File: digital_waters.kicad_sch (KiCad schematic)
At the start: 0 parts

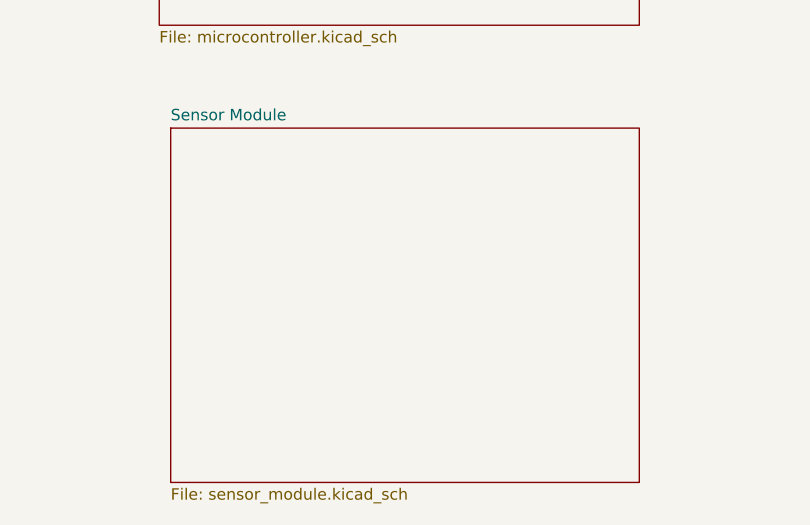
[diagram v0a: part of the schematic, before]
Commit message: Sensor board basic updates
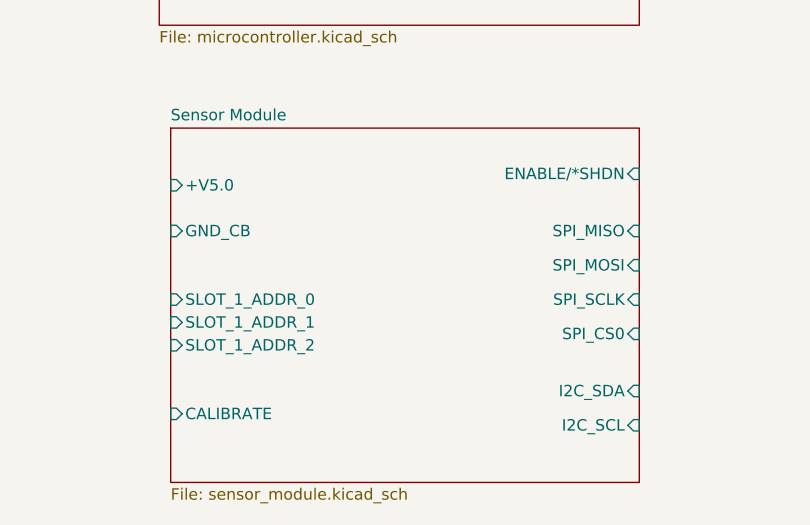
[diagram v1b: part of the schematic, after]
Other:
- sheet Sensor Module ports: added +V5.0, CALIBRATE, ENABLE/*SHDN, GND_CB, I2C_SCL, I2C_SDA, SLOT_1_ADDR_0, SLOT_1_ADDR_1, SLOT_1_ADDR_2, SPI_CS0, SPI_MISO, SPI_MOSI, SPI_SCLK; removed none
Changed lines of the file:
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@@
+			)
+		)
+		(pin "I2C_SDA" input
+			(at 179.07 110.49 0)
+			(effects
+				(font
+					(size 1.27 1.27)
+				)
+				(justify right)
+			)
+		)
+		(pin "I2C_SCL" input
+			(at 179.07 114.3 0)
+			(effects
+				(font
+					(size 1.27 1.27)
+				)
+				(justify right)
+			)
+		)
+		(pin "CALIBRATE" input
+			(at 127 113.03 180)
+			(effects
+				(font
+					(size 1.27 1.27)
+				)
+				(justify left)
+			)
+		)
+		(pin "SPI_SCLK" input
+			(at 179.07 100.33 0)
+			(effects
+				(font
+					(size 1.27 1.27)
+				)
+				(justify right)
+			)
+		)
+		(pin "SPI_CS0" input
+			(at 179.07 104.14 0)
+			(effects
+				(font
+					(size 1.27 1.27)
+				)
+				(justify right)
+			)
+		)
+		(pin "SPI_MOSI" input
+			(at 179.07 96.52 0)
+			(effects
+				(font
+					(size 1.27 1.27)
+				)
+				(justify right)
+			)
+		)
+		(pin "SPI_MISO" input
+			(at 179.07 92.71 0)
+			(effects
+				(font
+					(size 1.27 1.27)
+				)
+				(justify right)
+			)
+		)
+		(pin "GND_CB" input
+			(at 127 92.71 180)
+			(effects
+				(font
+					(size 1.27 1.27)
+				)
+				(justify left)
+			)
+		)
+		(pin "ENABLE{slash}*SHDN" input
+			(at 179.07 86.36 0)
+			(effects
+				(font
+					(size 1.27 1.27)
+				)
+				(justify right)
+			)
+		)
+		(pin "+V5.0" input
+			(at 127 87.63 180)
+			(effects
+				(font
+					(size 1.27 1.27)
+				)
+				(justify left)
+			)
+		)
+		(pin "SLOT_1_ADDR_0" input
+			(at 127 100.33 180)
+			(effects
+				(font
+					(size 1.27 1.27)
+				)
+				(justify left)
+			)
+		)
+		(pin "SLOT_1_ADDR_2" input
+			(at 127 105.41 180)
+			(effects
+				(font
+					(size 1.27 1.27)
+				)
+				(justify left)
+			)
+		)
+		(pin "SLOT_1_ADDR_1" input
+			(at 127 102.87 180)
+			(effects
+				(font
+					(size 1.27 1.27)
+				)
+				(justify left)
 			)
 		)

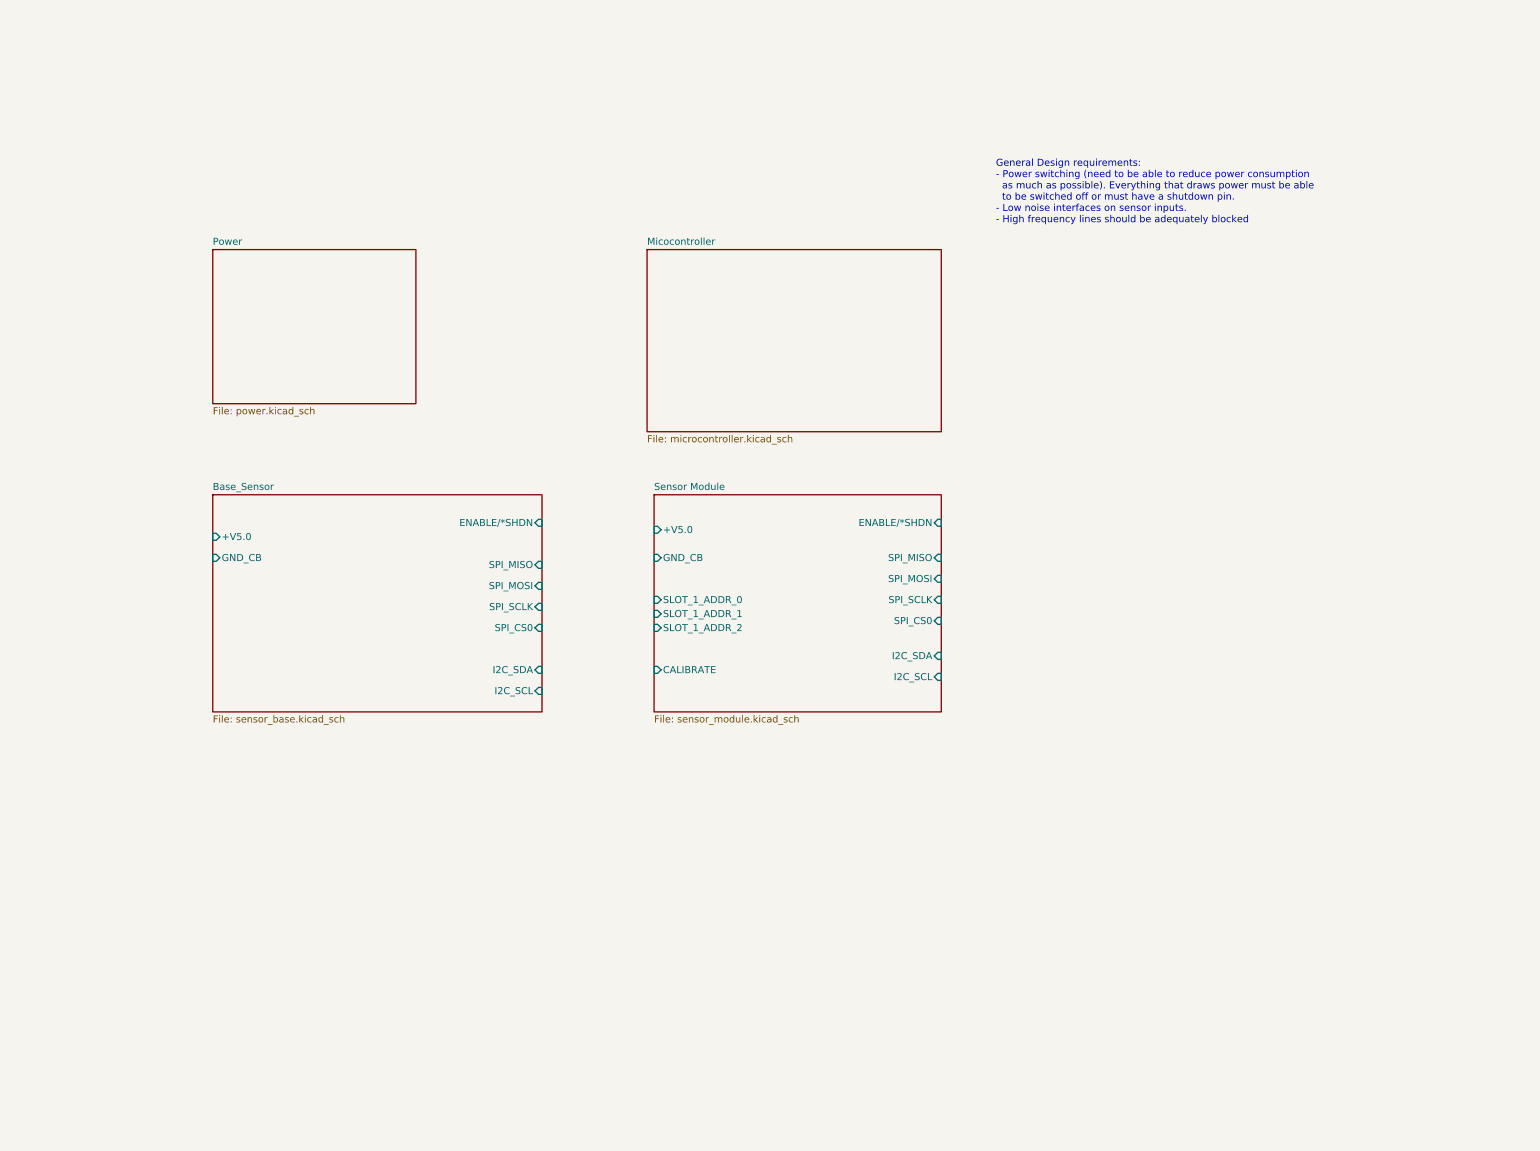
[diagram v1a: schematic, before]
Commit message: Split the sensor modules into a 4 and 8 port version. Fleshed out the power module a bit more. Started adding sensor board connectors to the root schematic and started pulling out sensor boards to their own, separate module. Began wiring up the root schematic to get my bearings a bit.
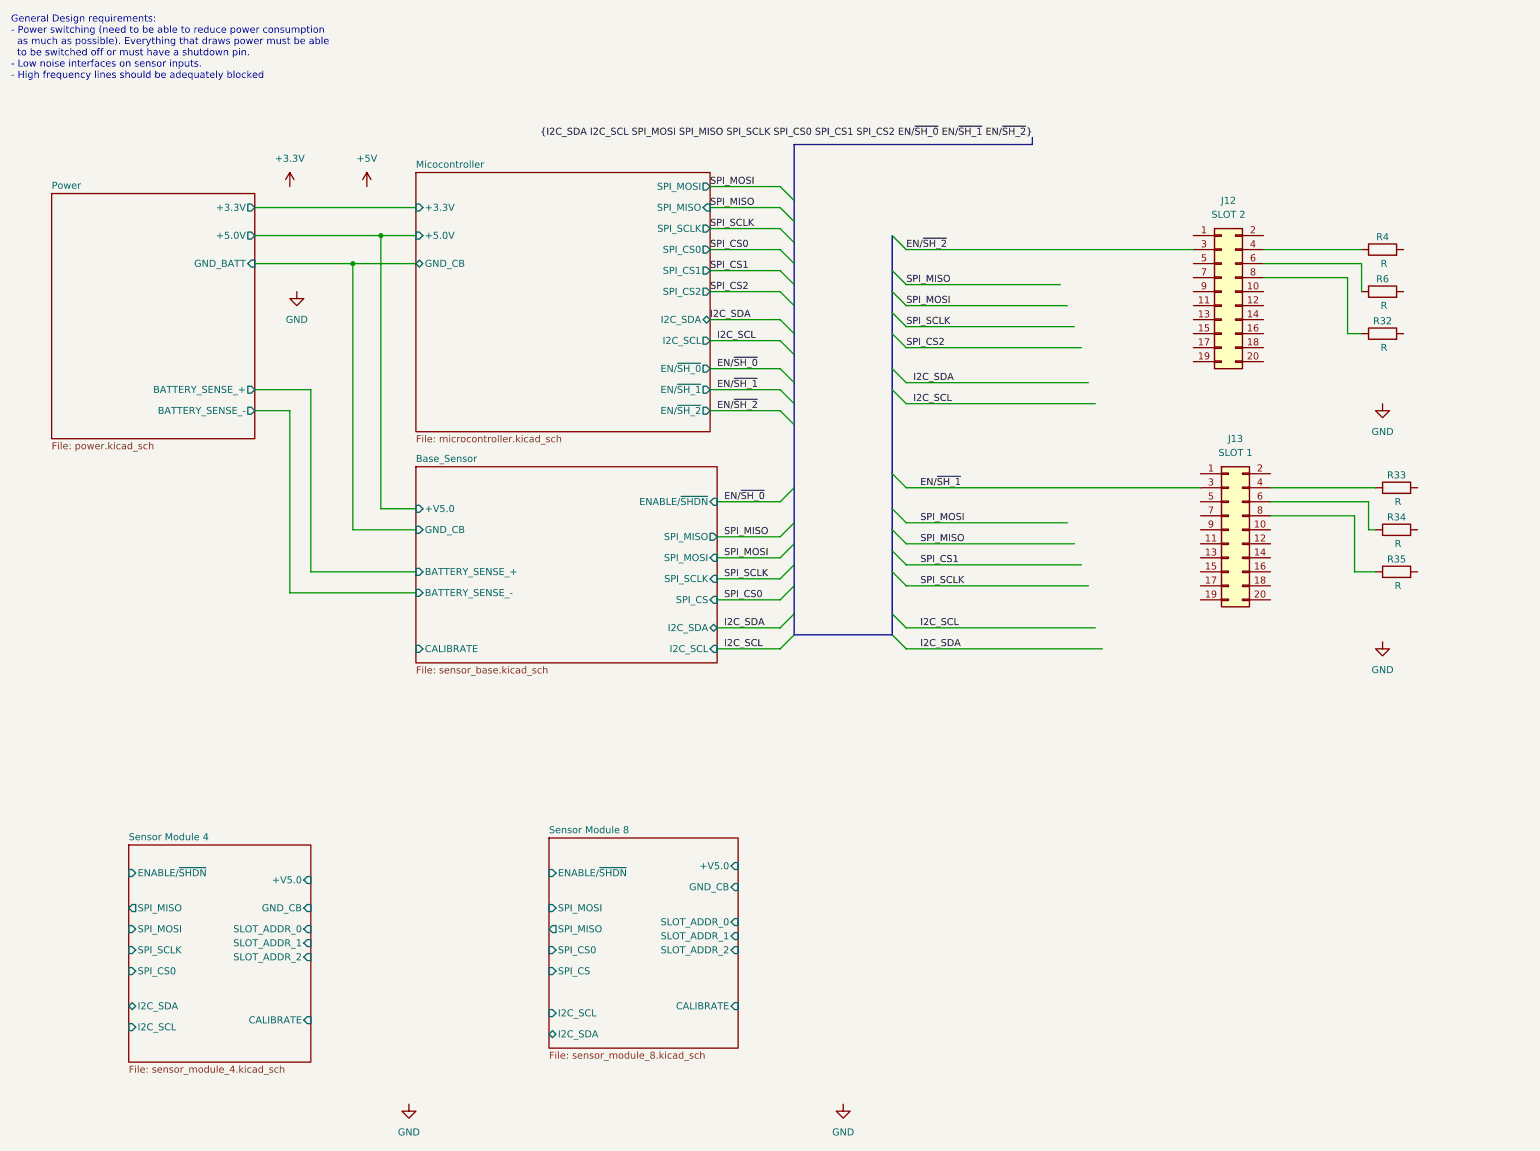
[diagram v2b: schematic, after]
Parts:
- added J12: SLOT 2, symbol Connector_Generic:Conn_02x10_Odd_Even
- added J13: SLOT 1, symbol Connector_Generic:Conn_02x10_Odd_Even
- added R32, R33, R34, R35, R4, R6: R, symbol Device:R
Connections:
- new net: J12.6 (Pin_6), R6.1
- new net: J13.8 (Pin_8), R35.1
- new net: J12.4 (Pin_4), R4.1
- new net: J12.8 (Pin_8), R32.1
- new net: J13.4 (Pin_4), R33.1
- new net: J13.6 (Pin_6), R34.1
- new net EN/~{SH_1}: J13.3 (Pin_3)
- new net EN/~{SH_2}: J12.3 (Pin_3)
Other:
- sheet Sensor Module renamed Sensor Module 4
- added sheet Sensor Module 8 (sensor_module_8.kicad_sch)
- sheet Base_Sensor ports: added BATTERY_SENSE_+, BATTERY_SENSE_-, CALIBRATE, ENABLE/~{SHDN}, SPI_CS; removed ENABLE/*SHDN, SPI_CS0
- sheet Micocontroller ports: added +3.3V, +5.0V, EN/~{SH_0}, EN/~{SH_1}, EN/~{SH_2}, GND_CB, I2C_SCL, I2C_SDA, SPI_CS0, SPI_CS1, SPI_CS2, SPI_MISO, SPI_MOSI, SPI_SCLK; removed none
- sheet Power ports: added +3.3V, +5.0V, BATTERY_SENSE_+, BATTERY_SENSE_-, GND_BATT; removed none
- sheet Sensor Module 4: file sensor_module.kicad_sch -> sensor_module_4.kicad_sch
- sheet Sensor Module 4 ports: added ENABLE/~{SHDN}, SLOT_ADDR_0, SLOT_ADDR_1, SLOT_ADDR_2; removed ENABLE/*SHDN, SLOT_1_ADDR_0, SLOT_1_ADDR_1, SLOT_1_ADDR_2

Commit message: Removed hierarchical labels on the sensor board (4 slot) in favour of local labels and connectors. The idea was that the sensor boards are plug-ins so having them defined as separate boards makes more sense. Eventually I think we'll pull them out of the main schematic and design each one separately with the common connector pinout.
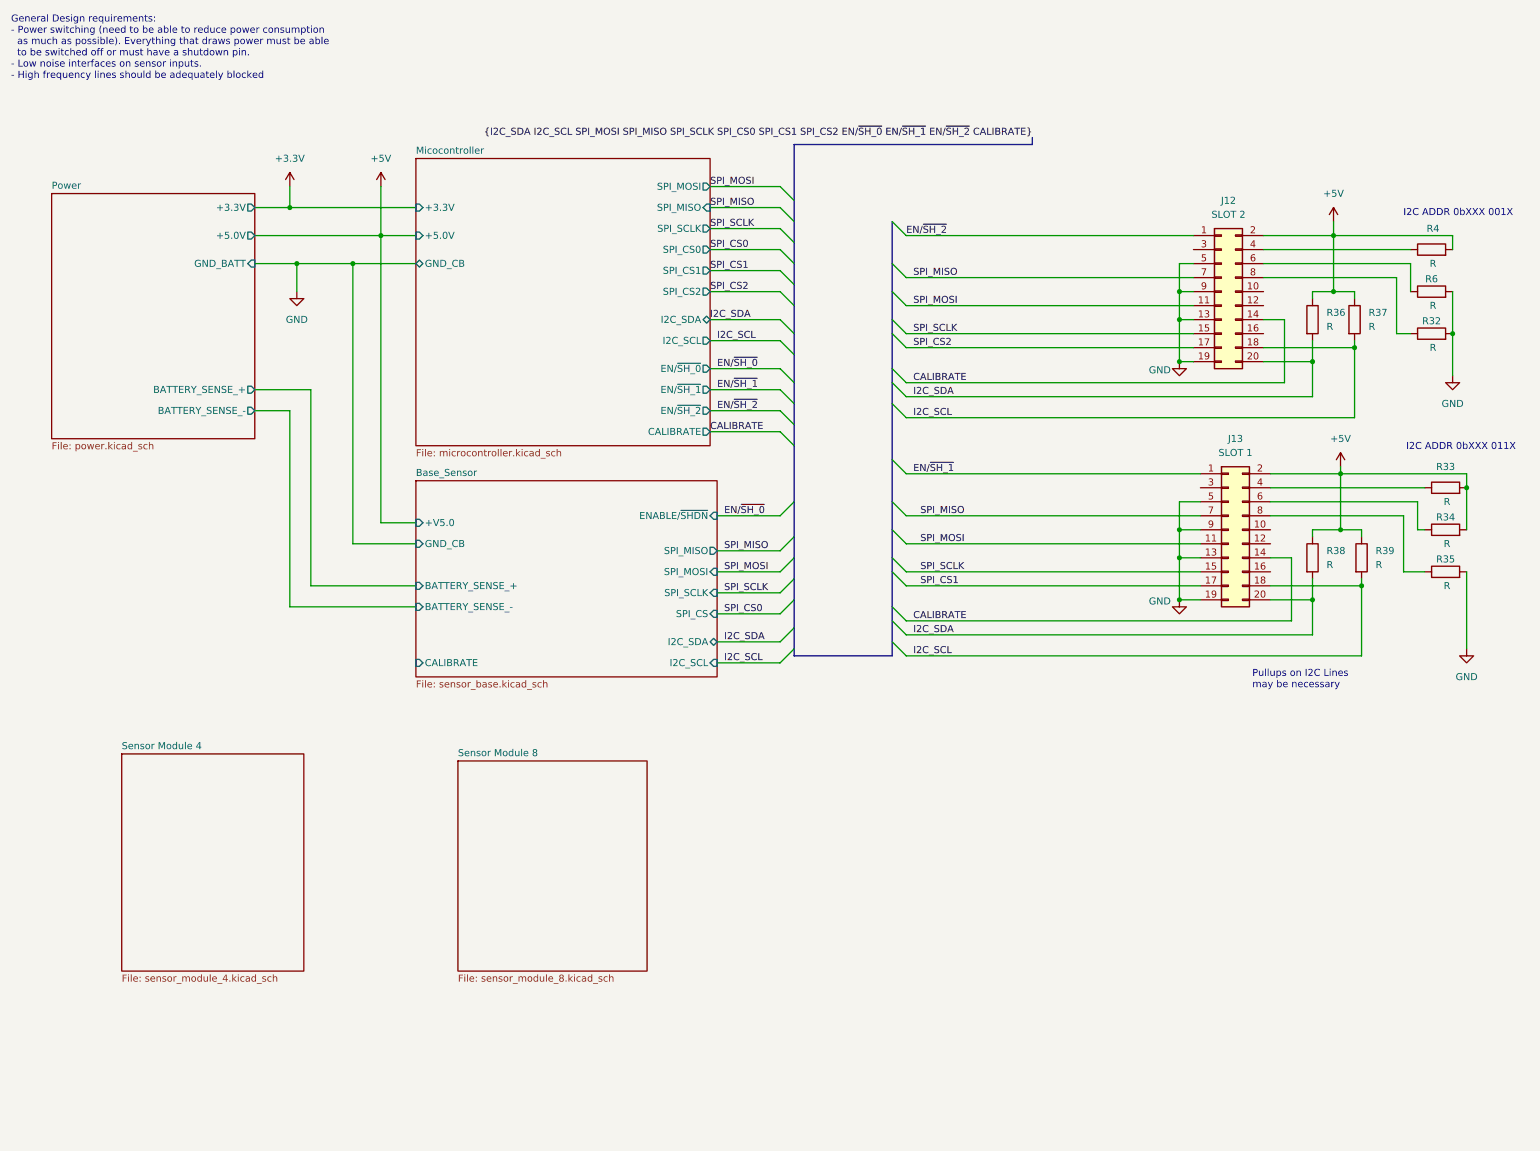
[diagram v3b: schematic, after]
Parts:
- added R36, R37, R38, R39: R, symbol Device:R
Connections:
- net +5V: now also J12.2 (Pin_2), J13.2 (Pin_2), R33.2, R34.2, R4.2, R36.1, R37.1, R38.1, R39.1
- net EN/~{SH_1}: now also J13.1 (Pin_1); no longer J13.3 (Pin_3)
- net EN/~{SH_2}: now also J12.1 (Pin_1); no longer J12.3 (Pin_3)
- net GND: now also J12.13 (Pin_13), J12.19 (Pin_19), J12.5 (Pin_5), J12.9 (Pin_9), J13.13 (Pin_13), J13.19 (Pin_19), J13.5 (Pin_5), J13.9 (Pin_9), R32.2, R35.2, R6.2
- net I2C_SCL: now also J12.18 (Pin_18), J13.18 (Pin_18), R37.2, R39.2
- net I2C_SDA: now also J12.20 (Pin_20), J13.20 (Pin_20), R36.2, R38.2
- net SPI_CS1: now also J13.17 (Pin_17)
- net SPI_CS2: now also J12.17 (Pin_17)
- net SPI_MISO: now also J12.7 (Pin_7), J13.7 (Pin_7)
- net SPI_MOSI: now also J12.11 (Pin_11), J13.11 (Pin_11)
- net SPI_SCLK: now also J12.15 (Pin_15), J13.15 (Pin_15)
- net CALIBRATE: now reaches J12.14 (Pin_14)
- net CALIBRATE: now also J13.14 (Pin_14)
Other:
- sheet Micocontroller ports: added CALIBRATE; removed none
- sheet Sensor Module 4 ports: added none; removed +V5.0, CALIBRATE, ENABLE/~{SHDN}, GND_CB, I2C_SCL, I2C_SDA, SLOT_ADDR_0, SLOT_ADDR_1, SLOT_ADDR_2, SPI_CS0, SPI_MISO, SPI_MOSI, SPI_SCLK
- sheet Sensor Module 8 ports: added none; removed +V5.0, CALIBRATE, ENABLE/~{SHDN}, GND_CB, I2C_SCL, I2C_SDA, SLOT_ADDR_0, SLOT_ADDR_1, SLOT_ADDR_2, SPI_CS, SPI_CS0, SPI_MISO, SPI_MOSI
- note added: "I2C ADDR 0bXXX 001X"
- note added: "I2C ADDR 0bXXX 011X"
- note added: "Pullups on I2C Lines may be necessary"
- moved on the sheet: R32, R33, R34, R35, R4, R6

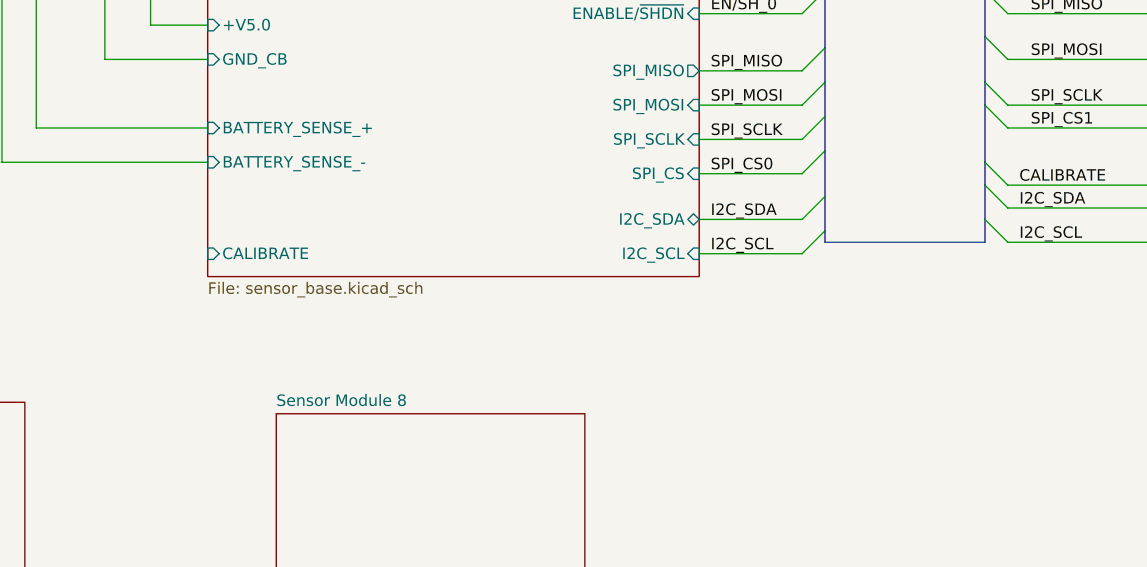
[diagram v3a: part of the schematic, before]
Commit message: Cleaned up some signal lines in the sensor board. Shuffled the decoupling caps around a bit as well as rearranged the EEPROM and power supply for clarity. Added buffered 2.5V offset to the pH and ORP circuits. Swapped one TBD input on the base sensor and sensor_4 boards for an ADC calibration input.
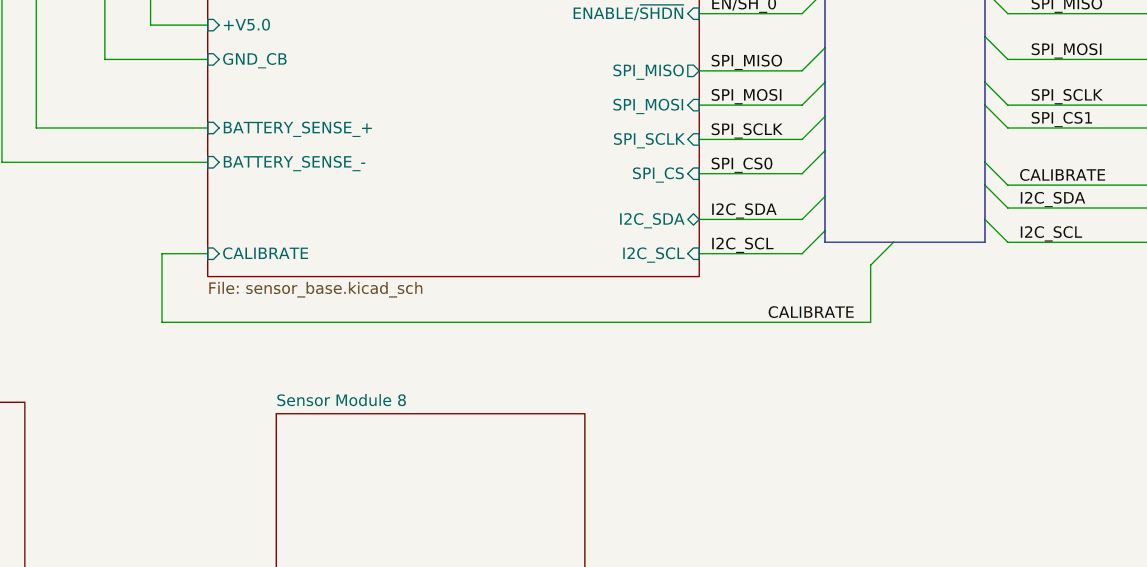
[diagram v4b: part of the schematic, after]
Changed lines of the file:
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@@
+	)
+	(bus_entry
+		(at 160.02 110.49)
+		(size -2.54 2.54)
+		(stroke
+			(width 0)
+			(type default)
+		)
 	)
 	(bus_entry
@@
 	(wire
 		(pts
+			(xy 78.74 119.38) (xy 78.74 111.76)
+		)
+		(stroke
+			(width 0)
+			(type default)
+		)
+	)
+	(wire
+		(pts
 			(xy 254 44.45) (xy 254 45.72)
 		)
@@
 		)
 	)
+	(bus
+		(pts
+			(xy 160.02 110.49) (xy 170.18 110.49)
+		)
+		(stroke
+			(width 0)
+			(type default)
+		)
+	)
 	(wire
 		(pts
@@
 	(bus
 		(pts
-			(xy 152.4 110.49) (xy 170.18 110.49)
+			(xy 152.4 110.49) (xy 160.02 110.49)
 		)
 		(stroke
@@
 	(wire
 		(pts
+			(xy 78.74 111.76) (xy 83.82 111.76)
+		)
+		(stroke
+			(width 0)
+			(type default)
+		)
+	)
+	(wire
+		(pts
 			(xy 137.16 25.4) (xy 149.86 25.4)
 		)
@@
 	(wire
 		(pts
+			(xy 157.48 119.38) (xy 78.74 119.38)
+		)
+		(stroke
+			(width 0)
+			(type default)
+		)
+	)
+	(wire
+		(pts
 			(xy 172.72 60.96) (xy 241.3 60.96)
+		)
+		(stroke
+			(width 0)
+			(type default)
+		)
+	)
+	(wire
+		(pts
+			(xy 157.48 113.03) (xy 157.48 119.38)
 		)
 		(stroke
@@
 		(effects
 			(font
+				(size 1.27 1.27)
+			)
+			(justify left bottom)
+		)
+	)
+	(label "CALIBRATE"
+		(at 146.05 119.38 0)
+		(effects
+			(font
